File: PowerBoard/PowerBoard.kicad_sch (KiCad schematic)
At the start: 107 parts, among them J1 V_IN, J10 GATE_PH_A, J11 GND, J12 V_IN, J13 TEMP_SENS, J2 PH_B, J3 PH_A, J4 PH_C, J5 CURR_SENS_PH_A, J6 CURR_SENS_PH_B, J7 CURR_SENS_PH_C, J8 GATE_PH_C, J9 GATE_PH_B, Q1 HSP0076A, Q10 HSP0076A, Q11 HSP0076A, Q12 HSP0076A, Q13 HSP0076A, Q14 HSP0076A, Q15 HSP0076A, Q16 HSP0076A, Q17 HSP0076A, Q18 HSP0076A, Q2 HSP0076A, Q3 HSP0076A, Q4 HSP0076A, Q5 HSP0076A, Q6 HSP0076A, Q7 HSP0076A, Q8 HSP0076A, Q9 HSP0076A

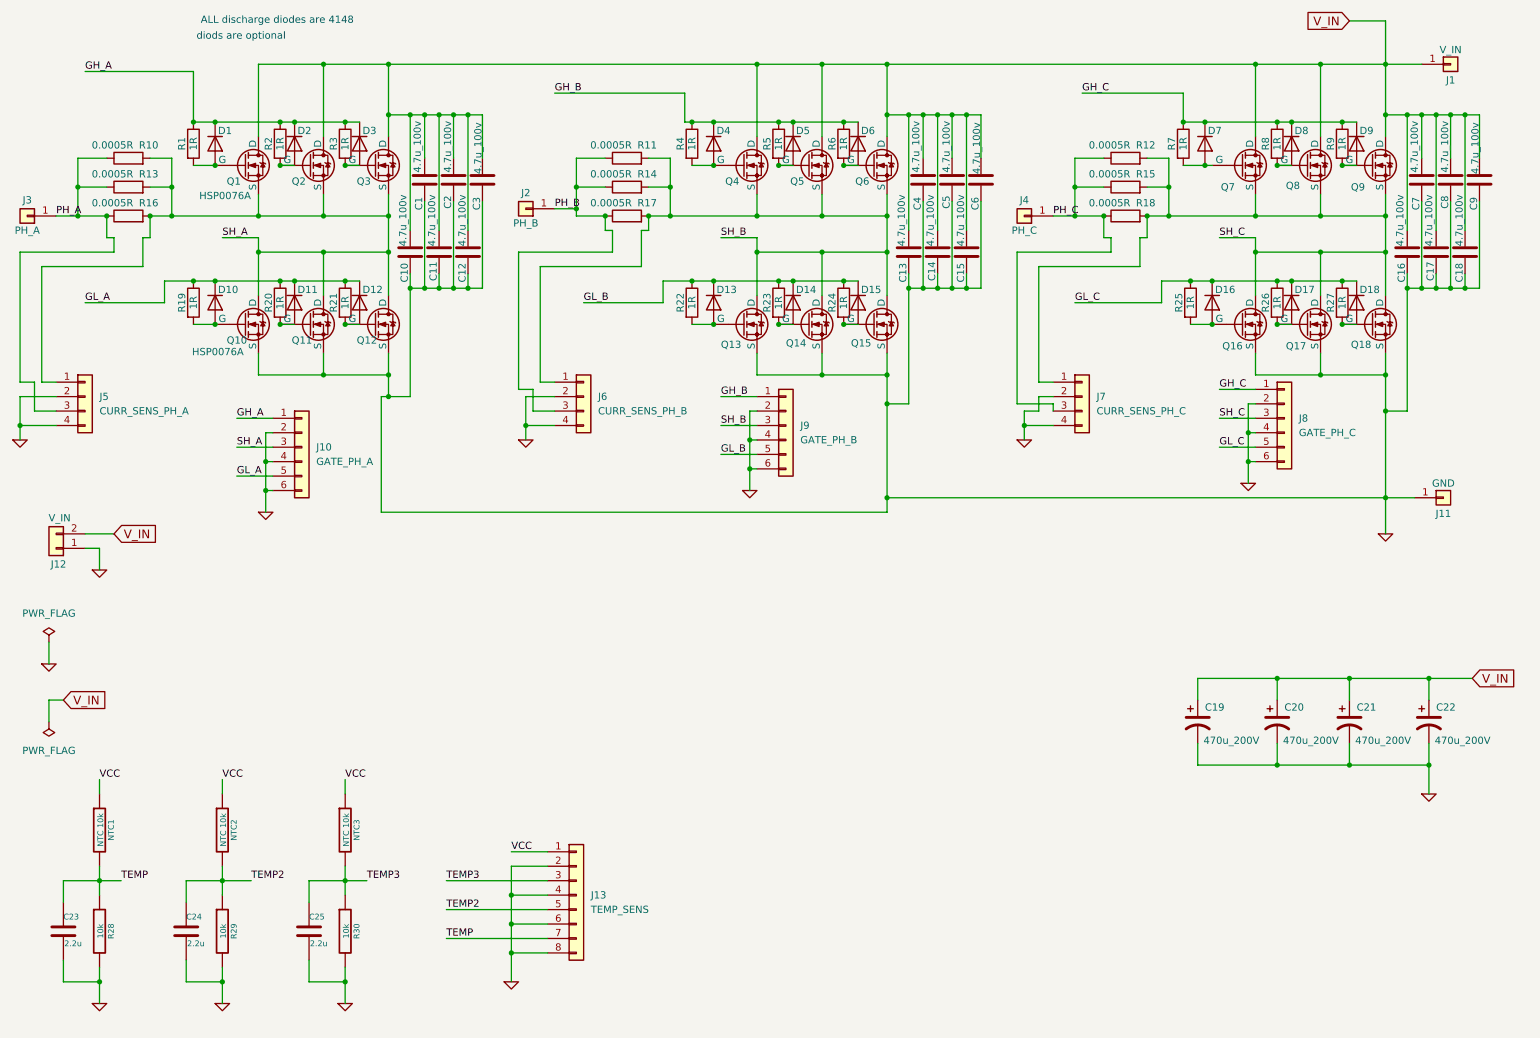
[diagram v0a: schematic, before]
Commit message: updated board for new mosfets
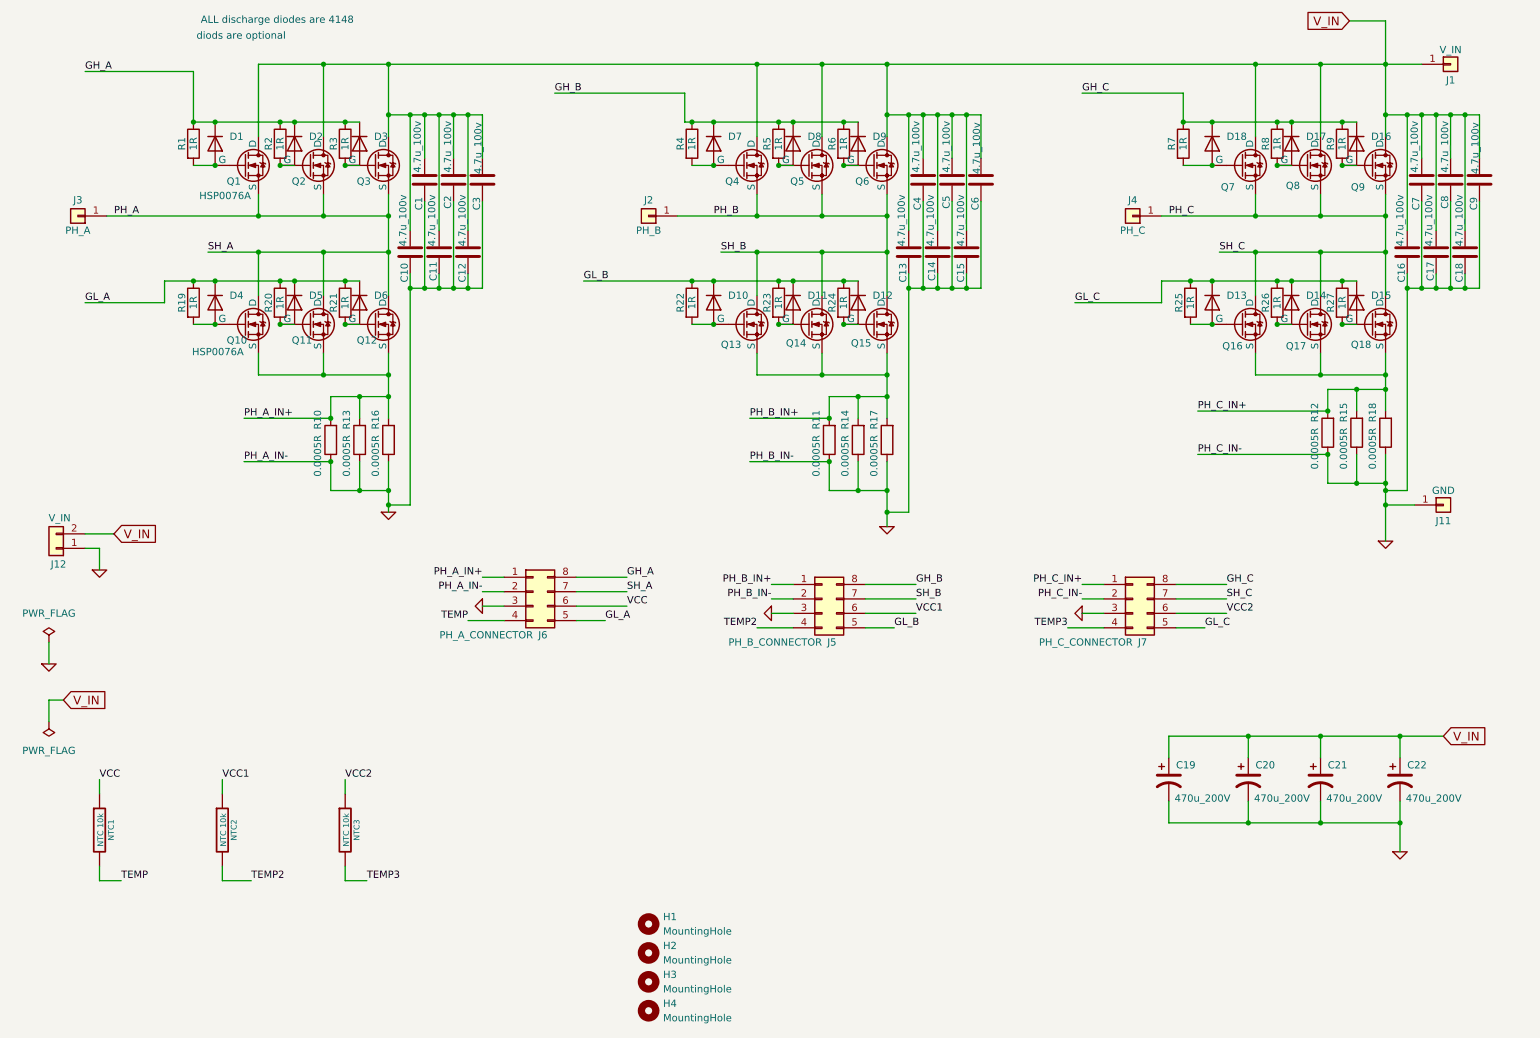
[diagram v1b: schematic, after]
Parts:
- removed C23, C24, C25: 2.2u, Capacitor_SMD:C_0603_1608Metric, symbol BLDC_4-rescue:C-RESCUE-BLDC_4
- removed J10: GATE_PH_A, Connector_PinHeader_1.00mm:PinHeader_1x06_P1.00mm_Vertical, symbol Connector_Generic:Conn_01x06
- removed J13: TEMP_SENS, Connector_PinHeader_1.00mm:PinHeader_1x08_P1.00mm_Vertical, symbol Connector_Generic:Conn_01x08
- removed J5: CURR_SENS_PH_A, Connector_PinHeader_1.00mm:PinHeader_1x04_P1.00mm_Vertical, symbol Connector_Generic:Conn_01x04
- removed J6: CURR_SENS_PH_B, Connector_PinHeader_1.00mm:PinHeader_1x04_P1.00mm_Vertical, symbol Connector_Generic:Conn_01x04
- removed J7: CURR_SENS_PH_C, Connector_PinHeader_1.00mm:PinHeader_1x04_P1.00mm_Vertical, symbol Connector_Generic:Conn_01x04
- removed J8: GATE_PH_C, Connector_PinHeader_1.00mm:PinHeader_1x06_P1.00mm_Vertical, symbol Connector_Generic:Conn_01x06
- removed J9: GATE_PH_B, Connector_PinHeader_1.00mm:PinHeader_1x06_P1.00mm_Vertical, symbol Connector_Generic:Conn_01x06
- removed R28, R29, R30: 10k, Resistor_SMD:R_0603_1608Metric, symbol BLDC_4-rescue:R-RESCUE-BLDC_4
- added H1, H2, H3, H4: MountingHole, MountingHole:MountingHole_2.2mm_M2, symbol Mechanical:MountingHole
- added J5: PH_B_CONNECTOR, Connector_PinHeader_2.54mm:PinHeader_2x04_P2.54mm_Vertical, symbol Connector_Generic:Conn_02x04_Counter_Clockwise
- added J6: PH_A_CONNECTOR, Connector_PinHeader_2.54mm:PinHeader_2x04_P2.54mm_Vertical, symbol Connector_Generic:Conn_02x04_Counter_Clockwise
- added J7: PH_C_CONNECTOR, Connector_PinHeader_2.54mm:PinHeader_2x04_P2.54mm_Vertical, symbol Connector_Generic:Conn_02x04_Counter_Clockwise
- J12: footprint Connector_PinHeader_1.00mm:PinHeader_1x02_P1.00mm_Vertical -> Connector_PinHeader_2.54mm:PinHeader_1x02_P2.54mm_Vertical
- Q1, Q10, Q11, Q12, Q13, Q14, Q15, Q16, Q17, Q18, Q2, Q3, Q4, Q5, Q6, Q7, Q8, Q9: footprint Package_TO_SOT_THT:TO-220-3_Horizontal_TabUp_withoutHole -> Package_TO_SOT_SMD:Infineon_PG-HSOF-8-1
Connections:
- net GH_A: now also J6.8 (Pin_8)
- net GH_B: now also D7.1 (K), D8.1 (K), D9.1 (K), J5.8 (Pin_8); no longer D4.1 (K), D5.1 (K), D6.1 (K)
- net GH_C: now also D16.1 (K), D17.1 (K), D18.1 (K), J7.8 (Pin_8); no longer D7.1 (K), D8.1 (K), D9.1 (K)
- net GL_A: now also D4.1 (K), D5.1 (K), D6.1 (K), J6.5 (Pin_5); no longer D10.1 (K), D11.1 (K), D12.1 (K)
- net GL_B: now also D10.1 (K), D11.1 (K), D12.1 (K), J5.5 (Pin_5); no longer D13.1 (K), D14.1 (K), D15.1 (K)
- net GL_C: now also D13.1 (K), D14.1 (K), D15.1 (K), J7.5 (Pin_5); no longer D16.1 (K), D17.1 (K), D18.1 (K)
- net GND: now also R10.1, R11.1, R12.1, R13.1, R14.1, R15.1, R16.1, R17.1, R18.1, J5.2 (Pin_2), J5.3 (Pin_3), J6.2 (Pin_2), J6.3 (Pin_3), J7.2 (Pin_2), J7.3 (Pin_3); no longer Q10.3 (S), Q11.3 (S), Q12.3 (S), Q13.3 (S), Q14.3 (S), Q15.3 (S), Q16.3 (S), Q17.3 (S), Q18.3 (S)
- net PH_A: now also Q1.2 (S), Q10.3 (D), Q11.3 (D), Q12.3 (D), Q2.2 (S), Q3.2 (S), J6.7 (Pin_7); no longer R10.1, R13.1, R16.1
- net PH_B: now also Q13.3 (D), Q14.3 (D), Q15.3 (D), Q4.2 (S), Q5.2 (S), Q6.2 (S), J5.7 (Pin_7); no longer R11.1, R14.1, R17.1
- net PH_C: now also Q16.3 (D), Q17.3 (D), Q18.3 (D), Q7.2 (S), Q8.2 (S), Q9.2 (S), J7.7 (Pin_7); no longer R12.1, R15.1, R18.1
- net TEMP: now also J6.4 (Pin_4)
- net TEMP2: now also J5.4 (Pin_4)
- net TEMP3: now also J7.4 (Pin_4)
- net VCC: now also J6.6 (Pin_6); no longer NTC2.1, NTC3.1
- net V_IN: now also Q1.3 (D), Q2.3 (D), Q3.3 (D), Q4.3 (D), Q5.3 (D), Q6.3 (D), Q7.3 (D), Q8.3 (D), Q9.3 (D); no longer Q1.2 (D), Q2.2 (D), Q3.2 (D), Q4.2 (D), Q5.2 (D), Q6.2 (D), Q7.2 (D), Q8.2 (D), Q9.2 (D)
- net at Q14.1 (G), R23.2: now also D11.2 (A); no longer D14.2 (A)
- net at Q9.1 (G), R9.2: now also D16.2 (A); no longer D9.2 (A)
- net at Q10.1 (G), R19.2: now also D4.2 (A); no longer D10.2 (A)
- net at Q18.1 (G), R27.2: now also D15.2 (A); no longer D18.2 (A)
- net at Q11.1 (G), R20.2: now also D5.2 (A); no longer D11.2 (A)
- net at Q6.1 (G), R6.2: now also D9.2 (A); no longer D6.2 (A)
- net at Q16.1 (G), R25.2: now also D13.2 (A); no longer D16.2 (A)
- net at Q12.1 (G), R21.2: now also D6.2 (A); no longer D12.2 (A)
- net at Q13.1 (G), R22.2: now also D10.2 (A); no longer D13.2 (A)
- net at Q7.1 (G), R7.2: now also D18.2 (A); no longer D7.2 (A)
- net at Q17.1 (G), R26.2: now also D14.2 (A); no longer D17.2 (A)
- net at Q15.1 (G), R24.2: now also D12.2 (A); no longer D15.2 (A)
- net at Q5.1 (G), R5.2: now also D8.2 (A); no longer D5.2 (A)
- net at Q4.1 (G), R4.2: now also D7.2 (A); no longer D4.2 (A)
- net at Q8.1 (G), R8.2: now also D17.2 (A); no longer D8.2 (A)
- net SH_A renamed PH_A_IN+
- net PH_A_IN+: now also J6.1 (Pin_1); no longer Q1.3 (S), Q2.3 (S), Q3.3 (S)
- net SH_B renamed PH_B_IN+
- net PH_B_IN+: now also J5.1 (Pin_1); no longer Q4.3 (S), Q5.3 (S), Q6.3 (S)
- net SH_C renamed PH_C_IN+
- net PH_C_IN+: now also J7.1 (Pin_1); no longer Q7.3 (S), Q8.3 (S), Q9.3 (S)
- new net VCC1: J5.6 (Pin_6), NTC2.1
- new net VCC2: J7.6 (Pin_6), NTC3.1
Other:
- moved on the sheet: C19, C20, C21, C22, J11, J2, J4, R10, R11, R12, R13, R14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

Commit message: added resistor for shunts
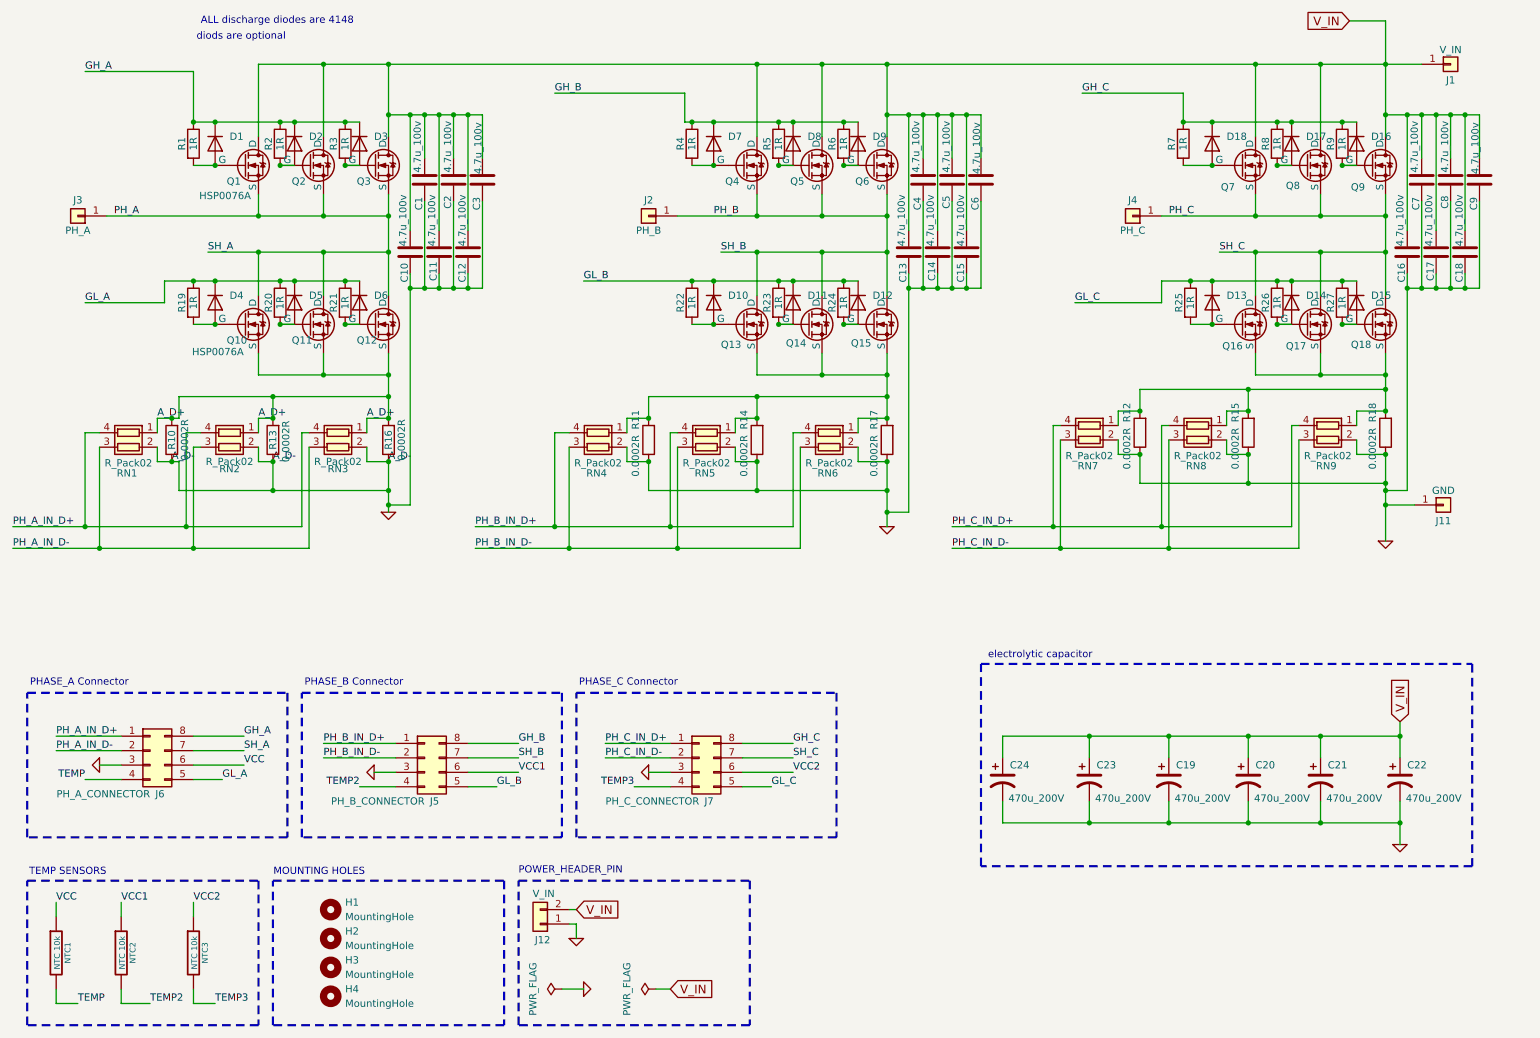
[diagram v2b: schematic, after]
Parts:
- added C23, C24: 470u_200V, Capacitor_THT:CP_Radial_D16.0mm_P7.50mm, symbol Device:C_Polarized_US
- added RN1, RN2, RN3, RN4, RN5, RN6, RN7, RN8, RN9: R_Pack02, Resistor_SMD:R_Array_Convex_2x0402, symbol Device:R_Pack02
- R10, R11, R12, R13, R14, R15, R16, R17, R18: value 0.0005R -> 0.0002R
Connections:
- net GND: now also C23.2, C24.2, RN1.2 (R2.1), RN2.2 (R2.1), RN3.2 (R2.1), RN4.2 (R2.1), RN5.2 (R2.1), RN6.2 (R2.1), RN7.2 (R2.1), RN8.2 (R2.1), RN9.2 (R2.1); no longer J5.2 (Pin_2), J6.2 (Pin_2), J7.2 (Pin_2)
- net V_IN: now also C23.1, C24.1
- net PH_A_IN+ renamed A_D+
- net A_D+: now also RN1.1 (R1.1), RN2.1 (R1.1), RN3.1 (R1.1); no longer J6.1 (Pin_1)
- net PH_B_IN+: no longer names the net of Q13.2 (S), Q14.2 (S), Q15.2 (S), R11.2, R14.2, R17.2
- net PH_B_IN+: now also RN4.1 (R1.1), RN5.1 (R1.1), RN6.1 (R1.1); no longer J5.1 (Pin_1)
- net PH_C_IN+: no longer names the net of Q16.2 (S), Q17.2 (S), Q18.2 (S), R12.2, R15.2, R18.2
- net PH_C_IN+: now also RN7.1 (R1.1), RN8.1 (R1.1), RN9.1 (R1.1); no longer J7.1 (Pin_1)
- new net PH_A_IN_D+: J6.1 (Pin_1), RN1.4 (R1.2), RN2.4 (R1.2), RN3.4 (R1.2)
- new net PH_A_IN_D-: J6.2 (Pin_2), RN1.3 (R2.2), RN2.3 (R2.2), RN3.3 (R2.2)
- new net PH_B_IN_D+: J5.1 (Pin_1), RN4.4 (R1.2), RN5.4 (R1.2), RN6.4 (R1.2)
- new net PH_B_IN_D-: J5.2 (Pin_2), RN4.3 (R2.2), RN5.3 (R2.2), RN6.3 (R2.2)
- new net PH_C_IN_D+: J7.1 (Pin_1), RN7.4 (R1.2), RN8.4 (R1.2), RN9.4 (R1.2)
- new net PH_C_IN_D-: J7.2 (Pin_2), RN7.3 (R2.2), RN8.3 (R2.2), RN9.3 (R2.2)
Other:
- note added: "MOUNTING HOLES"
- note added: "PHASE_A Connector"
- note added: "PHASE_B Connector"
- note added: "PHASE_C Connector"
- note added: "POWER_HEADER_PIN"
- note added: "TEMP SENSORS"
- note added: "electrolytic capacitor"
- moved on the sheet: H1, H2, H3, H4, J12, J5, J6, J7, NTC1, NTC2, NTC3, R10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

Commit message: new
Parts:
- removed RN1, RN2, RN3, RN4, RN5, RN6, RN7, RN8, RN9: R_Pack02, Resistor_SMD:R_Array_Convex_2x0402, symbol Device:R_Pack02
- added R28, R29, R30, R31, R32, R33, R34, R35, R36, R37, R38, R39, R40, R41, R42, R43, R44, R45: 10, Resistor_SMD:R_0201_0603Metric, symbol Device:R
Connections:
- net GND: now also R29.2, R31.2, R33.2, R35.2, R37.2, R39.2, R41.2, R43.2, R45.2
- net PH_A_IN_D+: now also R28.1, R30.1, R32.1
- net PH_A_IN_D-: now also R29.1, R31.1, R33.1
- net PH_B_IN_D+: now also R34.1, R36.1, R38.1
- net PH_B_IN_D-: now also R35.1, R37.1, R39.1
- net PH_C_IN_D+: now also R40.1, R42.1, R44.1
- net PH_C_IN_D-: now also R41.1, R43.1, R45.1
- net at Q13.2 (S), Q14.2 (S), Q15.2 (S)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: now also R34.2, R36.2, R38.2
- net at Q16.2 (S), Q17.2 (S), Q18.2 (S)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: now also R40.2, R42.2, R44.2
- net A_D+: no longer names the net of Q10.2 (S), Q11.2 (S), Q12.2 (S), R10.2, R13.2, R16.2
- net A_D+: now also R28.2, R30.2, R32.2

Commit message: power board is done !
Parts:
- removed C22, C23, C24: 470u_200V, Capacitor_THT:CP_Radial_D16.0mm_P7.50mm, symbol Device:C_Polarized_US
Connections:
- no-connect marks 0 -> 6
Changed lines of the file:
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@@
 		(color 0 0 0 0)
 	)
+	(no_connect
+		(at 186.69 153.67)
+	)
+	(no_connect
+		(at 186.69 146.05)
+	)
+	(no_connect
+		(at 201.93 146.05)
+	)
+	(no_connect
+		(at 256.54 153.67)
+	)
+	(no_connect
+		(at 201.93 153.67)
+	)
+	(no_connect
+		(at 256.54 146.05)
+	)
 	(wire
 		(pts
@@
 	)
 	(symbol
-		(lib_id "Device:C_Polarized_US")
-		(at 201.93 149.86 0)
-		(unit 1)
-		(exclude_from_sim no)
-		(in_bom yes)
-		(on_board yes)
-		(dnp no)
-		(property "Reference" "C23"
-			(at 203.2 147.32 0)
-			(effects
-				(font
-					(size 1.27 1.27)
-				)
-				(justify left)
-			)
-		)
-		(property "Value" "470u_200V"
-			(at 202.946 153.162 0)
-			(effects
-				(font
-					(size 1.27 1.27)
-				)
-				(justify left)
-			)
-		)
-		(property "Footprint" "Capacitor_THT:CP_Radial_D16.0mm_P7.50mm"
-			(at 201.93 149.86 0)
-			(effects
-				(font
-					(size 1.27 1.27)
-				)
-				(hide yes)
-			)
-		)
-		(property "Datasheet" "~"
-			(at 201.93 149.86 0)
-			(effects
-				(font
-					(size 1.27 1.27)
-				)
-				(hide yes)
-			)
-		)
-		(property "Description" "Polarized capacitor, US symbol"
-			(at 201.93 149.86 0)
-			(effects
-				(font
-					(size 1.27 1.27)
-				)
-				(hide yes)
-			)
-		)
-		(pin "2"
-		)
-		(pin "1"
-		)
-		(instances
-			(project "PowerBoard"
-				(path "/f0d46a6e-2214-493e-8380-6329d5bb9b12"
-					(reference "C23")
-					(unit 1)
-				)
-			)
-		)
-	)
-	(symbol
 		(lib_id "BLDC_4-rescue:GND-RESCUE-BLDC_4")
 		(at 166.37 105.41 0)
@@
 	)
 	(symbol
-		(lib_id "Device:C_Polarized_US")
-		(at 186.69 149.86 0)
-		(unit 1)
-		(exclude_from_sim no)
-		(in_bom yes)
-		(on_board yes)
-		(dnp no)
-		(property "Reference" "C24"
-			(at 187.96 147.32 0)
-			(effects
-				(font
-					(size 1.27 1.27)
-				)
-				(justify left)
-			)
-		)
-		(property "Value" "470u_200V"
-			(at 187.706 153.162 0)
-			(effects
-				(font
-					(size 1.27 1.27)
-				)
-				(justify left)
-			)
-		)
-		(property "Footprint" "Capacitor_THT:CP_Radial_D16.0mm_P7.50mm"
-			(at 186.69 149.86 0)
-			(effects
-				(font
-					(size 1.27 1.27)
-				)
-				(hide yes)
-			)
-		)
-		(property "Datasheet" "~"
-			(at 186.69 149.86 0)
-			(effects
-				(font
-					(size 1.27 1.27)
-				)
-				(hide yes)
-			)
-		)
-		(property "Description" "Polarized capacitor, US symbol"
-			(at 186.69 149.86 0)
-			(effects
-				(font
-					(size 1.27 1.27)
-				)
-				(hide yes)
-			)
-		)
-		(pin "2"
-		)
-		(pin "1"
-		)
-		(instances
-			(project "PowerBoard"
-				(path "/f0d46a6e-2214-493e-8380-6329d5bb9b12"
-					(reference "C24")
-					(unit 1)
-				)
-			)
-		)
-	)
-	(symbol
 		(lib_id "Connector_Generic:Conn_02x04_Counter_Clockwise")
 		(at 85.09 146.05 0)
@@
 					(unit 1)
 				)
-			)
-		)
-	)
-	(symbol
-		(lib_id "Device:C_Polarized_US")
-		(at 256.54 149.86 0)
-		(unit 1)
-		(exclude_from_sim no)
-		(in_bom yes)
-		(on_board yes)
-		(dnp no)
-		(property "Reference" "C22"
-			(at 257.81 147.32 0)
-			(effects
-				(font
-					(size 1.27 1.27)
-				)
-				(justify left)
-			)
-		)
-		(property "Value" "470u_200V"
-			(at 257.556 153.162 0)
-			(effects
-				(font
-					(size 1.27 1.27)
-				)
-				(justify left)
-			)
-		)
-		(property "Footprint" "Capacitor_THT:CP_Radial_D16.0mm_P7.50mm"
-			(at 256.54 149.86 0)
-			(effects
-				(font
-					(size 1.27 1.27)
-				)
-				(hide yes)
-			)
-		)
-		(property "Datasheet" "~"
-			(at 256.54 149.86 0)
-			(effects
-				(font
-					(size 1.27 1.27)
-				)
-				(hide yes)
-			)
-		)
-		(property "Description" "Polarized capacitor, US symbol"
-			(at 256.54 149.86 0)
-			(effects
-				(font
-					(size 1.27 1.27)
-				)
-				(hide yes)
-			)
-		)
-		(pin "2"
-		)
-		(pin "1"
-		)
-		(instances
-			(project "PowerBoard"
-				(path "/f0d46a6e-2214-493e-8380-6329d5bb9b12"
-					(reference "C22")
-					(unit 1)
-				)
